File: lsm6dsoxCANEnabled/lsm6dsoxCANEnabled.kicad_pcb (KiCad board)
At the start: 4 copper layers, 49.3 x 47.9 mm, 38 parts, among them J1 Termination Resistor, J2 GPIO, J3 Power, J4 SWD, J5 CANH and CANL input n output, SW1 Nrst, SW2 BOOT0, U2 TJA1051T, U3 STM32F103C8Tx, U4 AMS1117CD-3.3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

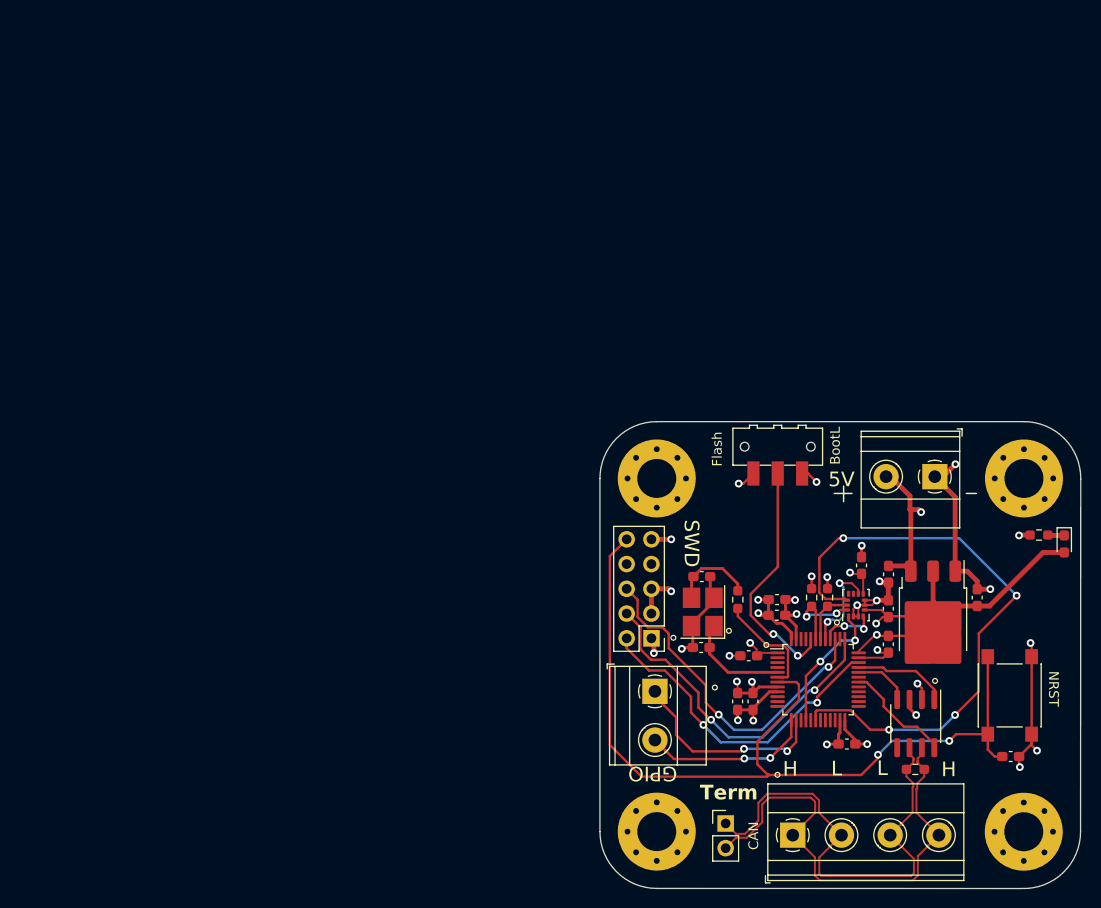
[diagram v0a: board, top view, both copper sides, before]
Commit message: redid the traces for the LSM6DSOX CAN PCB. Also created the BOM and the CPL files for manufacturing. Which means this board should be ready to get sent to pcb manufacturing.
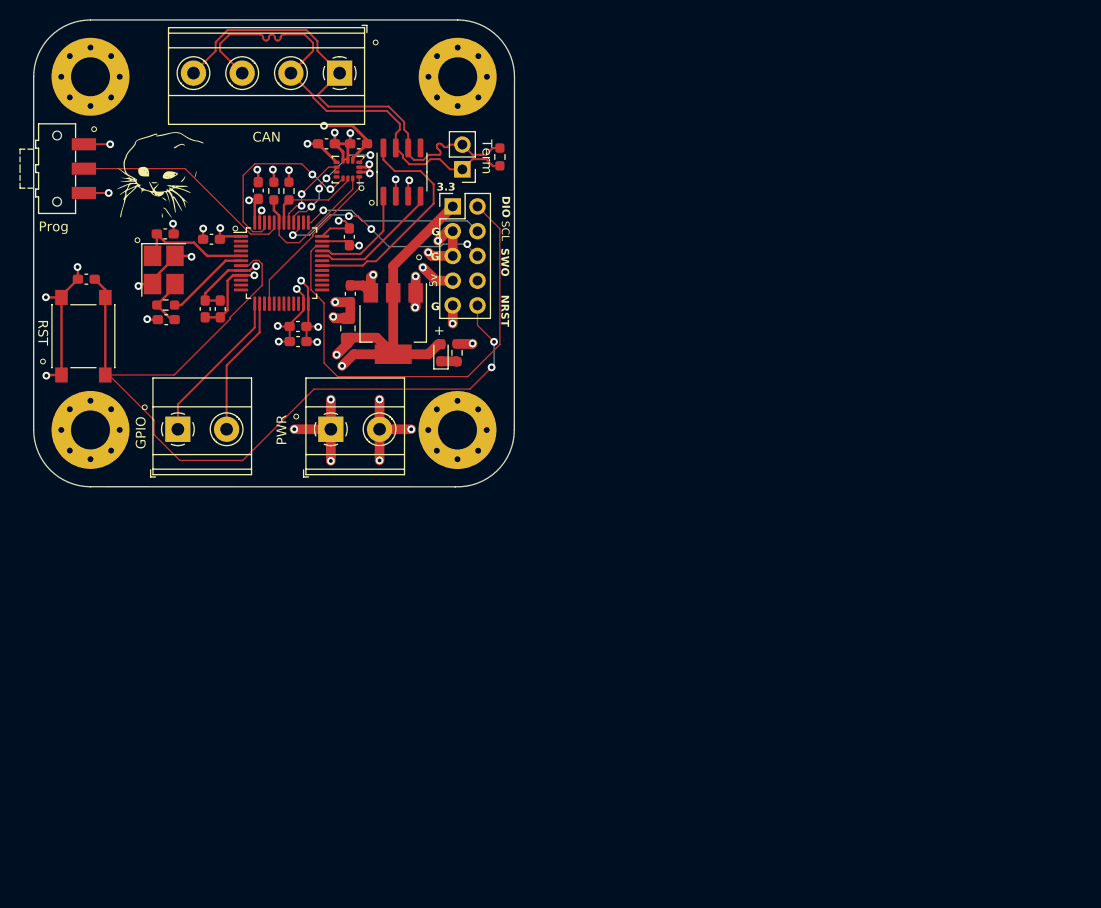
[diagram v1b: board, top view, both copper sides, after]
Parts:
- removed U4: AMS1117CD-3.3, Package_TO_SOT_SMD:TO-252-3_TabPin2
- added U5: AMS1117-3.3, Package_TO_SOT_SMD:SOT-223-3_TabPin2, F.Cu at (91.1, 50.8)
- C2, C3: value C -> 14p
- C5: footprint Capacitor_SMD:C_0603_1608Metric_Pad1.08x0.95mm_HandSolder -> Capacitor_SMD:C_0805_2012Metric_Pad1.18x1.45mm_HandSolder
- G***: moved to F.Cu
- R1, R2: value 10k -> 2k2
- Y1: value Crystal_GND24 -> 16mhz
- moved C1 106.8 mm to (59.6, 46.2), turned to 180 degrees
- moved G*** 103.9 mm to (66.9, 35.3), turned to 0 degrees
- moved SW1 102.0 mm to (59.3, 52.0), turned to 90 degrees
- moved J5 91.0 mm to (85.6, 25.0), turned to 180 degrees
- moved C8 79.7 mm to (77.2, 37.1), turned to 90 degrees
- moved SW2 79.3 mm to (56.6, 34.9), turned to -90 degrees
- moved U2 77.4 mm to (92.0, 35.2), turned to 90 degrees
- moved R4 76.0 mm to (102.0, 33.6), turned to 90 degrees
- moved C13 74.9 mm to (84.2, 32.3), turned to 0 degrees
- moved C9 72.9 mm to (86.6, 41.9), turned to -90 degrees
- moved J1 72.4 mm to (98.2, 34.9), turned to 180 degrees
- moved G*** 72.0 mm to (76.2, 41.9)
- moved H1 71.3 mm to (60.0, 25.4)
- moved H2 71.3 mm to (60.0, 61.7)
- moved H3 71.3 mm to (97.7, 25.4)
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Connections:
- J1 pad 1: CAN- -> CAN_IN+
- J1 pad 2: CAN+ -> CAN_IN-
- J2 pad 1: GPIO2 -> GPIO1
- J2 pad 2: GPIO1 -> GPIO2
- J4 pad 7: unconnected-(J4-Pin_7-Pad7) -> +5V
- J5 pad 1: CAN+ -> CAN_IN-
- J5 pad 2: CAN- -> CAN_IN+
- J5 pad 3: CAN- -> CAN_IN+
- J5 pad 4: CAN+ -> CAN_IN-
- R4 pad 1: CAN- -> CAN_IN+
- R4 pad 2: CAN+ -> CAN_IN-
- U2 pad 6: CAN- -> CAN_IN-
- U2 pad 7: CAN+ -> CAN_IN+
- U3 pad 18: CS -> unconnected-(U3-PB0-Pad18)
- U3 pad 46: unconnected-(U3-PB9-Pad46) -> CS
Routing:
- net CAN_IN-: track 0.00 -> 48.8 mm
- net CAN+: track 48.8 -> 0.00 mm
- net CAN_IN+: track 0.00 -> 48.7 mm
- net CAN-: track 48.1 -> 0.00 mm
- net CS: track 61.8 -> 20.4 mm, vias 4 -> 2
- net SYS_JTCK_SWCL: track 35.3 -> 18.8 mm, vias 2 -> 1
- net SYS_JTMS_SWDIO: track 33.5 -> 48.5 mm, vias 2 -> 0
- net +3.3V: track 68.9 -> 82.4 mm, vias 13 -> 14
- net Silent_Mode: track 11.2 -> 23.5 mm
- net SYS_JTDO_TRACESWO: track 35.5 -> 23.4 mm, vias 2 -> 4
- net CAN_RX: track 5.81 -> 13.4 mm
- net INT1: track 5.90 -> 13.4 mm, vias 2 -> 4
- net GPIO2: track 21.2 -> 14.3 mm, vias 2 -> 0
- net I2C1_SDA: track 9.23 -> 15.1 mm, vias 2 -> 0
- net I2C1_SCL: track 5.71 -> 9.63 mm
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- added copper zone on In2.Cu, net +3.3V
- added copper zone on In2.Cu, net +5V
- added copper zone on In1.Cu, net GND
- removed copper zone on In1.Cu, net +3.3V
- removed copper zone on In1.Cu, net +5V
- removed copper zone on In2.Cu, net GND
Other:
- board size 49.3 x 47.9 mm -> 49.4 x 47.9 mm
- board text added: "+"
- board text added: "3.3"
- board text added: "5v"
- board text added: "DIO"
- board text added: "G"
- board text added: "INPUT"
- board text added: "OUTPUT"
- board text added: "PA3"
- board text added: "PA4"
- board text added: "PWR"
- board text added: "Prog"
- board text added: "REV 1"
- board text added: "RST"
- board text added: "SCL"
- board text added: "SWO"
- board text removed: "5V"
- board text removed: "BootL"
- board text removed: "Flash"
- board text removed: "Rev 1"
- board text removed: "SWD"
